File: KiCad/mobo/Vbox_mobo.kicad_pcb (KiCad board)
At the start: 2 copper layers, 33.1 x 114.3 mm, 38 parts, among them J1 Conn_01x02, J2 JTAG_TC2030, J3 DuPont Connector, J4 Conn_01x06, J5 Conn_01x06, J6 Conn_01x10, J7 Conn_01x10, SW1 Boot, U1 XC6206, U2 X05A26H12G, U3 RP2040, U4 W25Q128JVS, Y1 12MHz

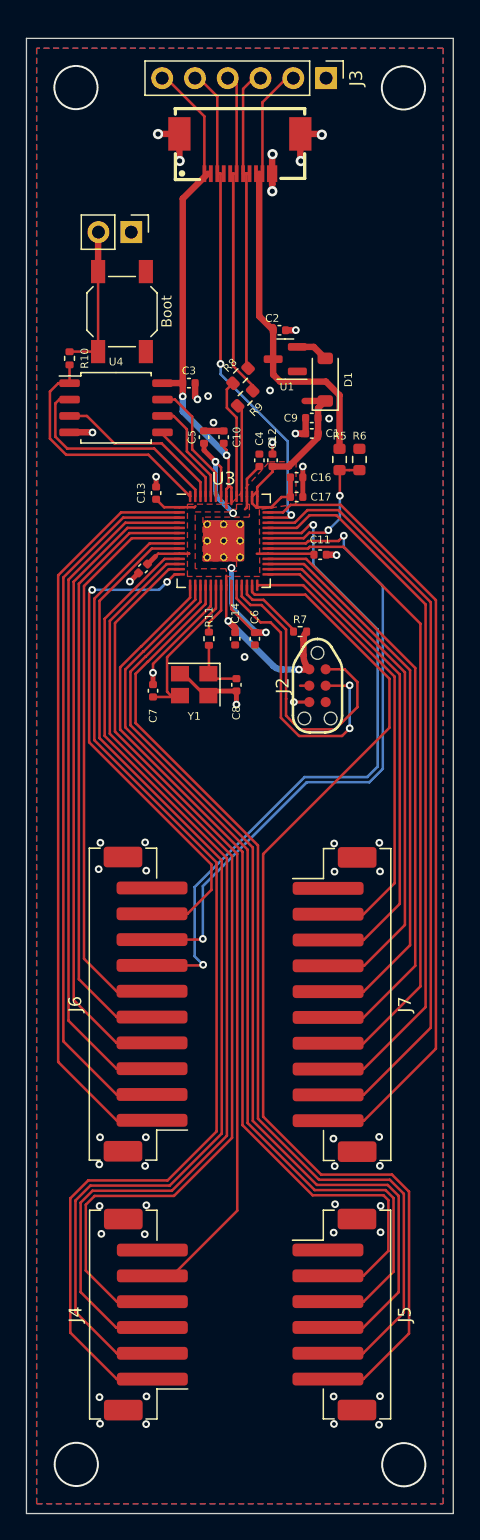
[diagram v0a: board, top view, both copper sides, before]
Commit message: replace vias with mounting holes
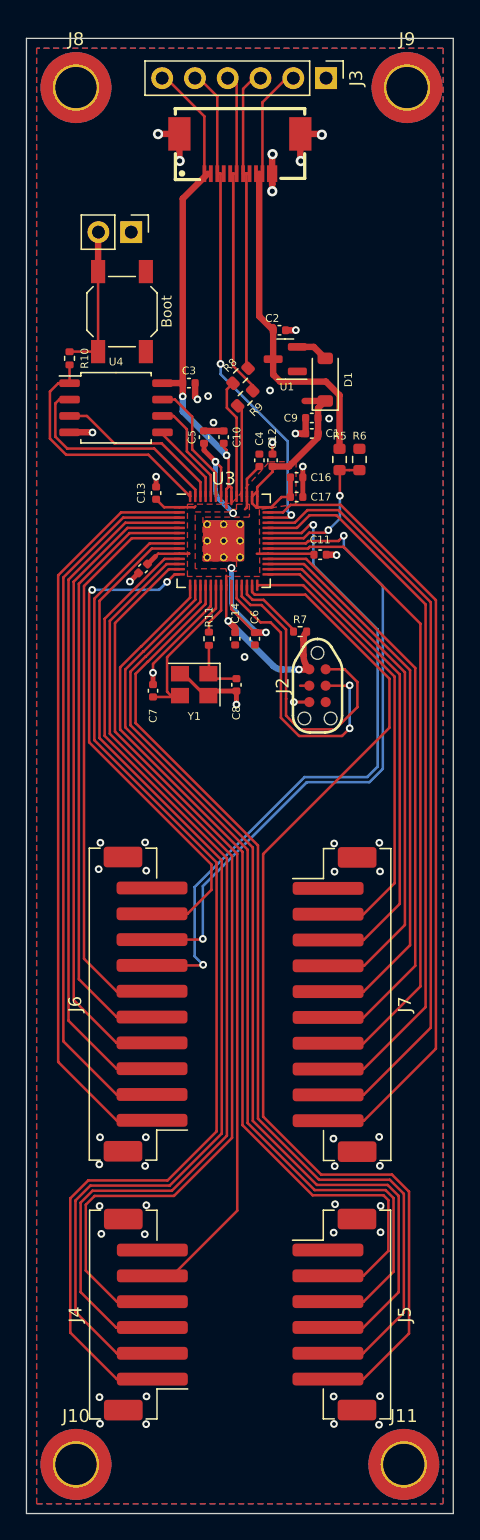
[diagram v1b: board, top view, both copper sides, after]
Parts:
- added J10: Conn_01x01, MountingHole:MountingHole_3.2mm_M3_ISO14580_Pad_TopBottom, F.Cu at (88.9, 152.4)
- added J11: Conn_01x01, MountingHole:MountingHole_3.2mm_M3_ISO14580_Pad_TopBottom, F.Cu at (114.3, 152.4)
- added J8: Conn_01x01, MountingHole:MountingHole_3.2mm_M3_ISO14580_Pad_TopBottom, F.Cu at (88.9, 45.7)
- added J9: Conn_01x01, MountingHole:MountingHole_3.2mm_M3_ISO14580_Pad_TopBottom, F.Cu at (114.6, 45.7)
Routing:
- net GND: vias 59 -> 55

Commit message: fix drc errors
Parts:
- moved R8 0.14 mm to (101.5, 68.1)
- moved J4 0.09 mm to (94.3, 140.7)
- moved J5 0.09 mm to (108.9, 140.7)
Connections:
- J4 pad MP: (no net) -> GND
- J5 pad MP: (no net) -> GND
- J6 pad MP: (no net) -> GND
- J7 pad MP: (no net) -> GND
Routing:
- net 3vDiode: track 88.2 -> 101.1 mm, vias 4 -> 5
- net ~{RESET}: track 6.31 -> 10.9 mm
- net GND: vias 55 -> 59

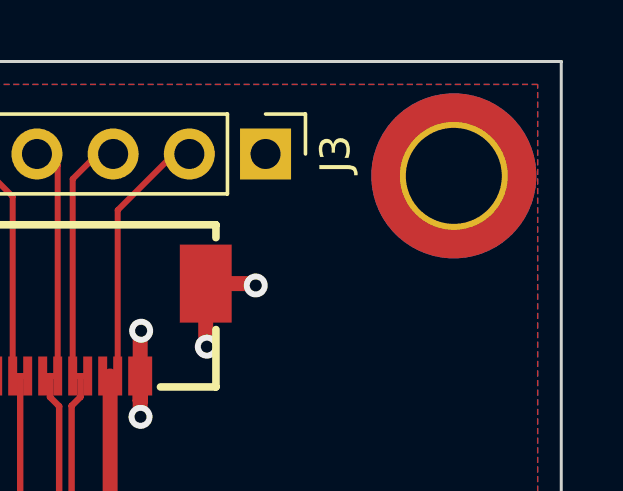
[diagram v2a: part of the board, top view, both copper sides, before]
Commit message: adjust mounting hole position
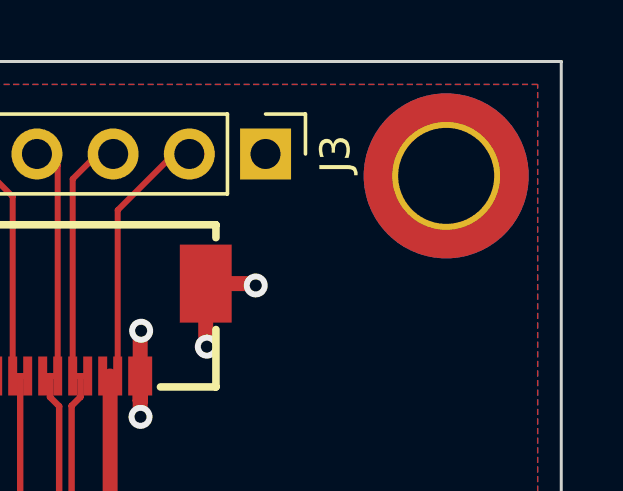
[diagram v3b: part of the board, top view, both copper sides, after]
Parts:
- moved J9 0.25 mm to (114.3, 45.7)
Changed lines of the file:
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@@
   )
   (footprint "MountingHole:MountingHole_3.2mm_M3_ISO14580_Pad_TopBottom" (layer "F.Cu")
-    (at 114.554 45.72)
+    (at 114.3 45.72)
     (descr "Mounting Hole 3.2mm, M3, ISO14580")
     (tags "mounting hole 3.2mm m3 iso14580")

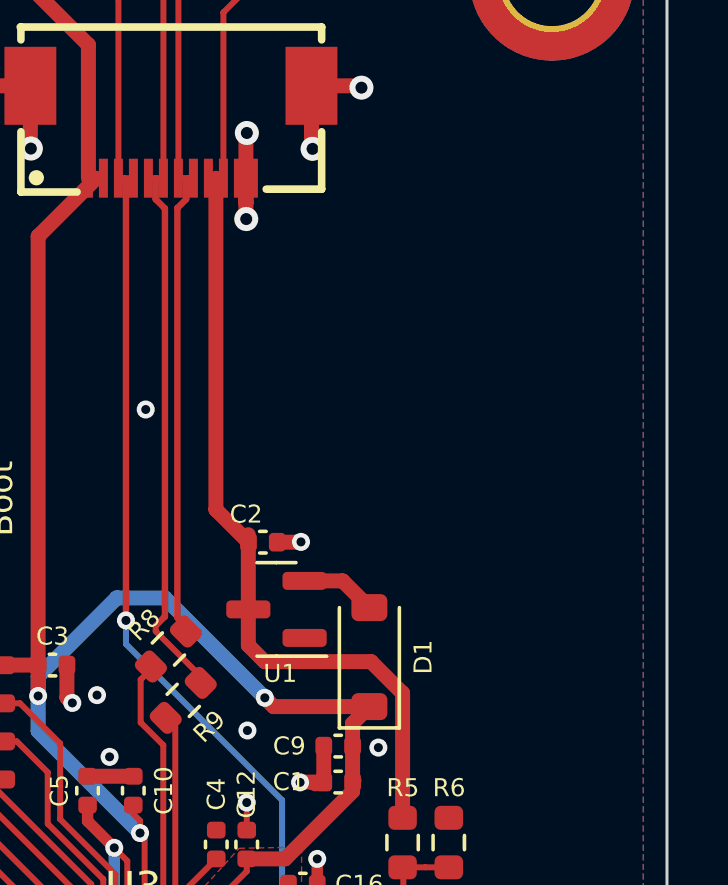
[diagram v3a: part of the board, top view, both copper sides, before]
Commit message: add 4 3.3v power headers
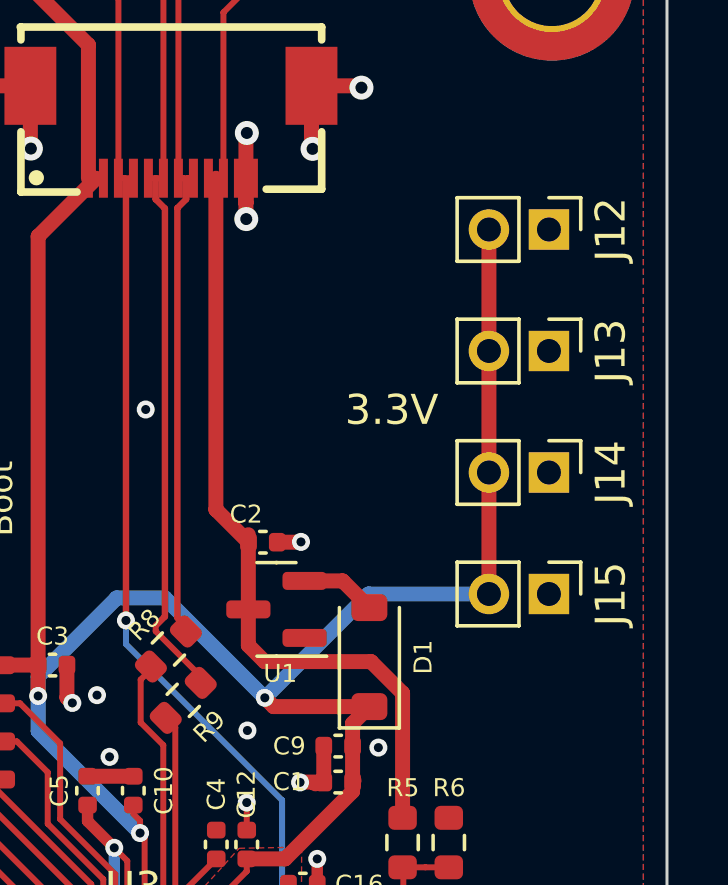
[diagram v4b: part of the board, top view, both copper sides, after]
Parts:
- added J12: Conn_01x02, Connector_PinHeader_2.00mm:PinHeader_1x02_P2.00mm_Vertical, F.Cu at (114.2, 54.1)
- added J13: Conn_01x02, Connector_PinHeader_2.00mm:PinHeader_1x02_P2.00mm_Vertical, F.Cu at (114.2, 58.2)
- added J14: Conn_01x02, Connector_PinHeader_2.00mm:PinHeader_1x02_P2.00mm_Vertical, F.Cu at (114.2, 62.2)
- added J15: Conn_01x02, Connector_PinHeader_2.00mm:PinHeader_1x02_P2.00mm_Vertical, F.Cu at (114.2, 66.3)
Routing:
- net 3vDiode: track 101.1 -> 122.2 mm
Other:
- board text added: "3.3V"
- board text added: "Conn_01x06"

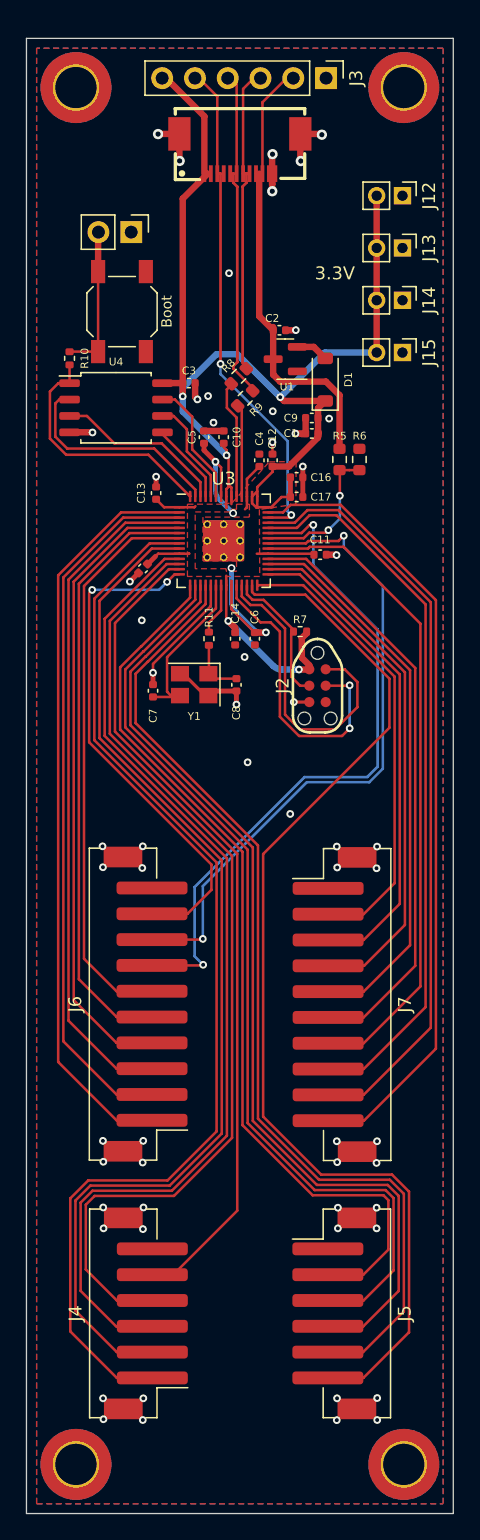
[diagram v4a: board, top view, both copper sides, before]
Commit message: realign the connectors
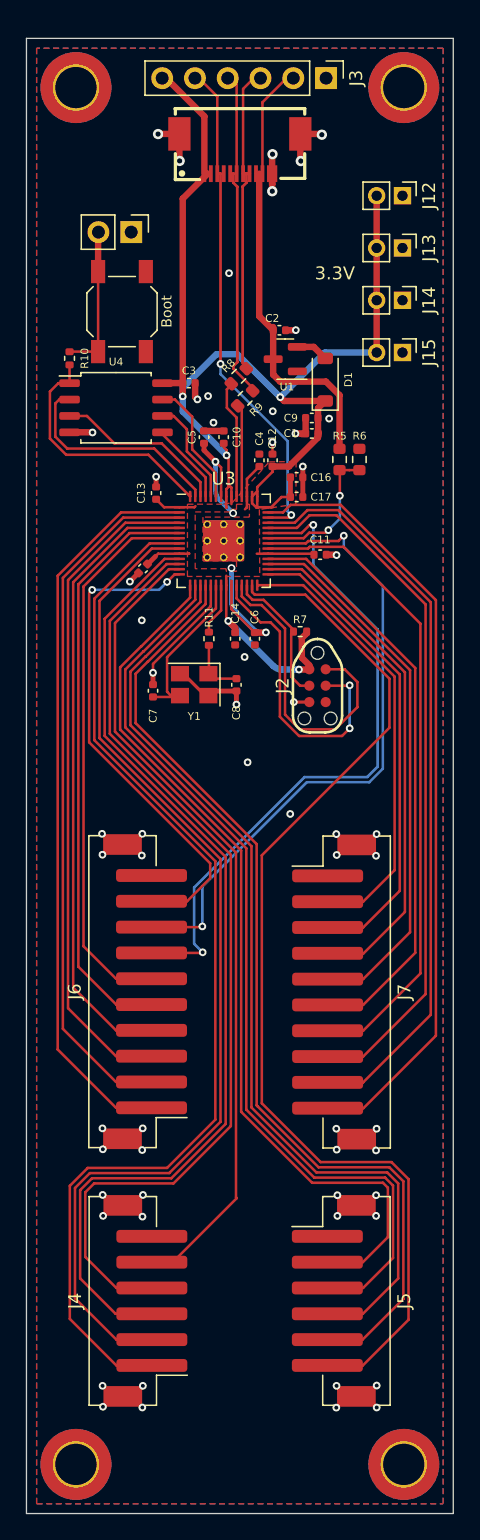
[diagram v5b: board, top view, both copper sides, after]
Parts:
- moved J4 0.97 mm to (94.3, 139.7)
- moved J6 0.97 mm to (94.3, 115.8)
- moved J7 0.97 mm to (108.9, 115.8)
- moved J5 0.97 mm to (108.9, 139.7)
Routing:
- net INDEX2: track 39.9 -> 38.9 mm
- net M1: track 85.2 -> 84.2 mm
- net M3: track 78.7 -> 77.7 mm
- net M4: track 75.8 -> 74.8 mm
- net M2: track 82.4 -> 81.3 mm
- net C_LT: track 73.2 -> 72.2 mm
- net A: track 75.4 -> 74.4 mm
- net C_UP: track 71.1 -> 70.1 mm
- net M5: track 64.8 -> 63.9 mm
- net R: track 59.0 -> 58.1 mm
- net UP: track 35.8 -> 34.9 mm
- net X: track 46.4 -> 45.4 mm
- net UP2: track 55.4 -> 54.5 mm
- net RING2: track 51.2 -> 50.2 mm
- net Z: track 40.8 -> 39.8 mm
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
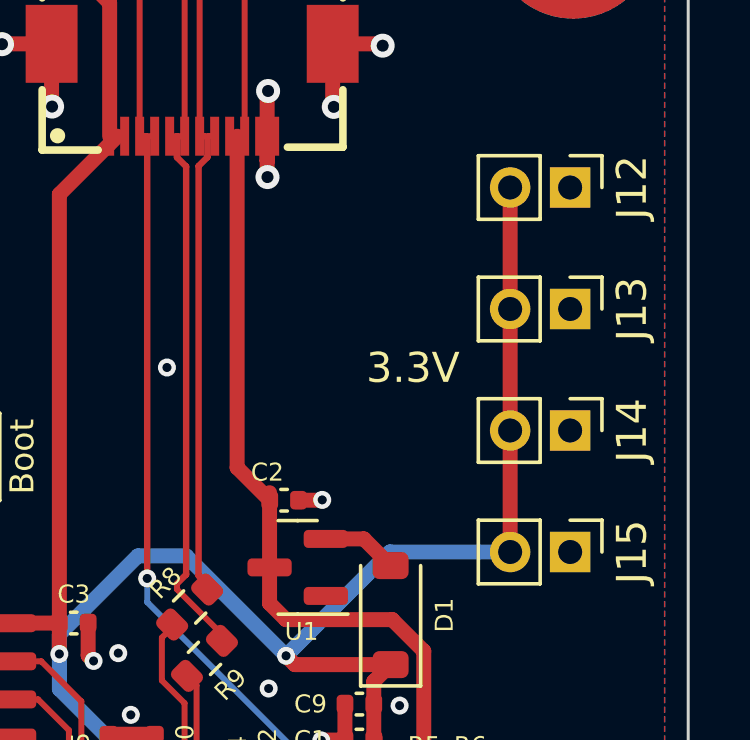
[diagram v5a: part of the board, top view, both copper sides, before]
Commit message: reroute the power for the 3.3v headers
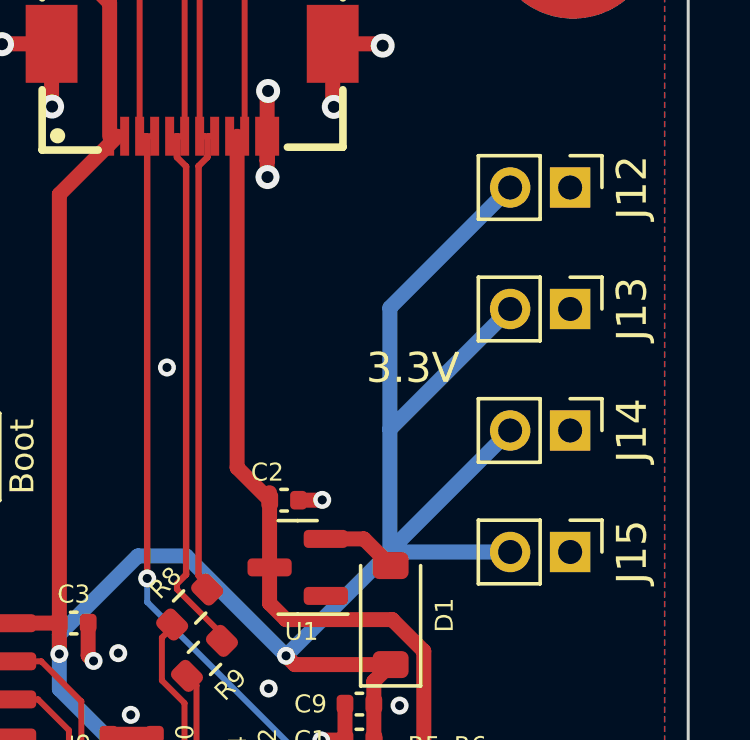
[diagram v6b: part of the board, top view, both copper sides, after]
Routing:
- net 3vDiode: track 122.2 -> 135.2 mm
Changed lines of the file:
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@@
   (segment (start 102.945599 77.400901) (end 102.945599 78.199651) (width 0.2) (layer "F.Cu") (net 53))
   (segment (start 100.69835 87.045419) (end 100.545601 86.892669) (width 0.2) (layer "F.Cu") (net 53))
-  (segment (start 112.2 62.2) (end 112.199999 58.150001) (width 0.5) (layer "F.Cu") (net 53))
   (segment (start 102.945599 77.400901) (end 102.9456 76.675382) (width 0.2) (layer "F.Cu") (net 53))
   (segment (start 101.2346 87.581669) (end 101.2346 87.946651) (width 0.5) (layer "F.Cu") (net 53))
@@
   (segment (start 106.7756 88.000714) (end 106.7756 87.8734) (width 0.5) (layer "F.Cu") (net 53))
   (segment (start 100.5456 78.256667) (end 100.57135 78.282417) (width 0.2) (layer "F.Cu") (net 53))
-  (segment (start 112.199999 58.150001) (end 112.2 54.1) (width 0.5) (layer "F.Cu") (net 53))
   (segment (start 98.849886 52.390805) (end 99.1108 52.390805) (width 0.2) (layer "F.Cu") (net 53))
   (segment (start 108.215601 70.003401) (end 105.023401 70.003401) (width 0.5) (layer "F.Cu") (net 53))
@@
   (segment (start 95.265368 81.838401) (end 95.065868 82.0379) (width 0.2) (layer "F.Cu") (net 53))
   (segment (start 98.849886 52.390805) (end 98.849886 47.949125) (width 0.5) (layer "F.Cu") (net 53))
-  (segment (start 112.199999 66.250001) (end 112.2 62.2) (width 0.5) (layer "F.Cu") (net 53))
   (segment (start 104.12735 75.493633) (end 104.12735 75.079417) (width 0.2) (layer "F.Cu") (net 53))
   (segment (start 99.1108 52.390805) (end 99.350013 52.390805) (width 0.2) (layer "F.Cu") (net 53))
@@
   (segment (start 104.73 69.71) (end 101.401015 66.381015) (width 0.5) (layer "B.Cu") (net 53))
   (segment (start 97.173716 68.998038) (end 97.173716 69.649001) (width 0.5) (layer "B.Cu") (net 53))
+  (segment (start 108.189999 58.110001) (end 108.189999 62.160001) (width 0.5) (layer "B.Cu") (net 53))
   (segment (start 100.69835 87.045419) (end 104.173439 90.520508) (width 0.5) (layer "B.Cu") (net 53))
   (segment (start 104.73 69.71) (end 108.189999 66.250001) (width 0.5) (layer "B.Cu") (net 53))
+  (segment (start 112.199999 58.150001) (end 108.189999 62.160001) (width 0.5) (layer "B.Cu") (net 53))
   (segment (start 101.401015 66.381015) (end 99.790739 66.381015) (width 0.5) (layer "B.Cu") (net 53))
+  (segment (start 112.2 54.1) (end 108.189999 58.110001) (width 0.5) (layer "B.Cu") (net 53))
   (segment (start 104.880546 90.8134) (end 106.178339 90.8134) (width 0.5) (layer "B.Cu") (net 53))
   (segment (start 97.173716 69.649001) (end 97.173716 70.820783) (width 0.5) (layer "B.Cu") (net 53))
+  (segment (start 108.189999 62.160001) (end 108.189999 66.210001) (width 0.5) (layer "B.Cu") (net 53))
+  (segment (start 108.189999 66.210001) (end 108.189999 66.250001) (width 0.5) (layer "B.Cu") (net 53))
   (segment (start 99.790739 66.381015) (end 97.173716 68.998038) (width 0.5) (layer "B.Cu") (net 53))
+  (segment (start 112.2 62.2) (end 108.189999 66.210001) (width 0.5) (layer "B.Cu") (net 53))
   (segment (start 108.189999 66.250001) (end 112.199999 66.250001) (width 0.5) (layer "B.Cu") (net 53))
   (arc (start 104.173439 90.520508) (mid 104.497862 90.73728) (end 104.880546 90.8134) (width 0.5) (layer "B.Cu") (net 53))
